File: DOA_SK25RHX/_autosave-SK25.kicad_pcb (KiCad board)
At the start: 2 copper layers, 29.2 x 29.2 mm, 44 parts, among them J1 Imput-, J2 Input+, J3 V+, J4 Output, J5 V-, J6 GND, Q1 BC560C, Q10 BD140, Q2 KSA992, Q3 KSA992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

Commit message: crude placement
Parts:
- D3: footprint LED_THT:LED_D5.0mm -> LED_THT:LED_D3.0mm
- Q10, Q9: footprint Package_TO_SOT_THT:TO-220-3_Vertical -> TAC:to225_std
- moved C2 91.7 mm to (181.6, 77.5), turned to 180 degrees
- moved D5 90.5 mm to (163.8, 115.6), turned to 180 degrees
- moved Q10 76.8 mm to (158.9, 84.5)
- moved D6 74.0 mm to (154.3, 72.4)
- moved Q9 68.9 mm to (158.8, 106.0), turned to 180 degrees
- moved R9 68.3 mm to (171.4, 108.0), turned to 90 degrees
- moved R10 67.3 mm to (177.2, 98.4), turned to 90 degrees
- moved Q3 66.8 mm to (157.5, 92.7), turned to 270 degrees
- moved Q7 63.8 mm to (160.7, 102.9), turned to 90 degrees
- moved Q8 62.0 mm to (152.4, 95.2), turned to 90 degrees
- moved RV5 60.5 mm to (146.1, 77.5), turned to 180 degrees
- moved R11 60.3 mm to (177.2, 92.1), turned to 90 degrees
- moved C1 59.8 mm to (165.1, 84.5), turned to 270 degrees
- moved Q6 57.6 mm to (161.3, 96.5)
- moved RV4 56.7 mm to (156.8, 78.1), turned to 180 degrees
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
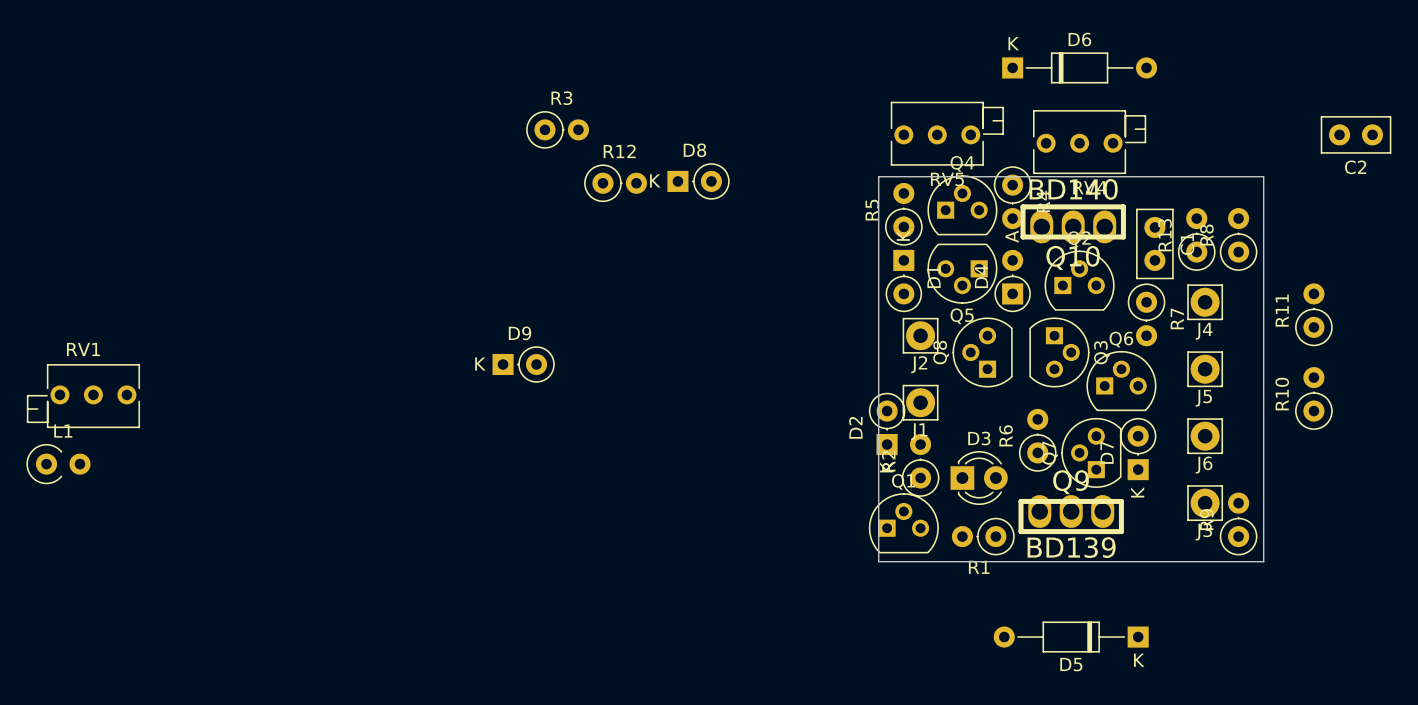
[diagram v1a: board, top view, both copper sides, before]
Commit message: abandoned layout. just TAC schematics for DOA socket
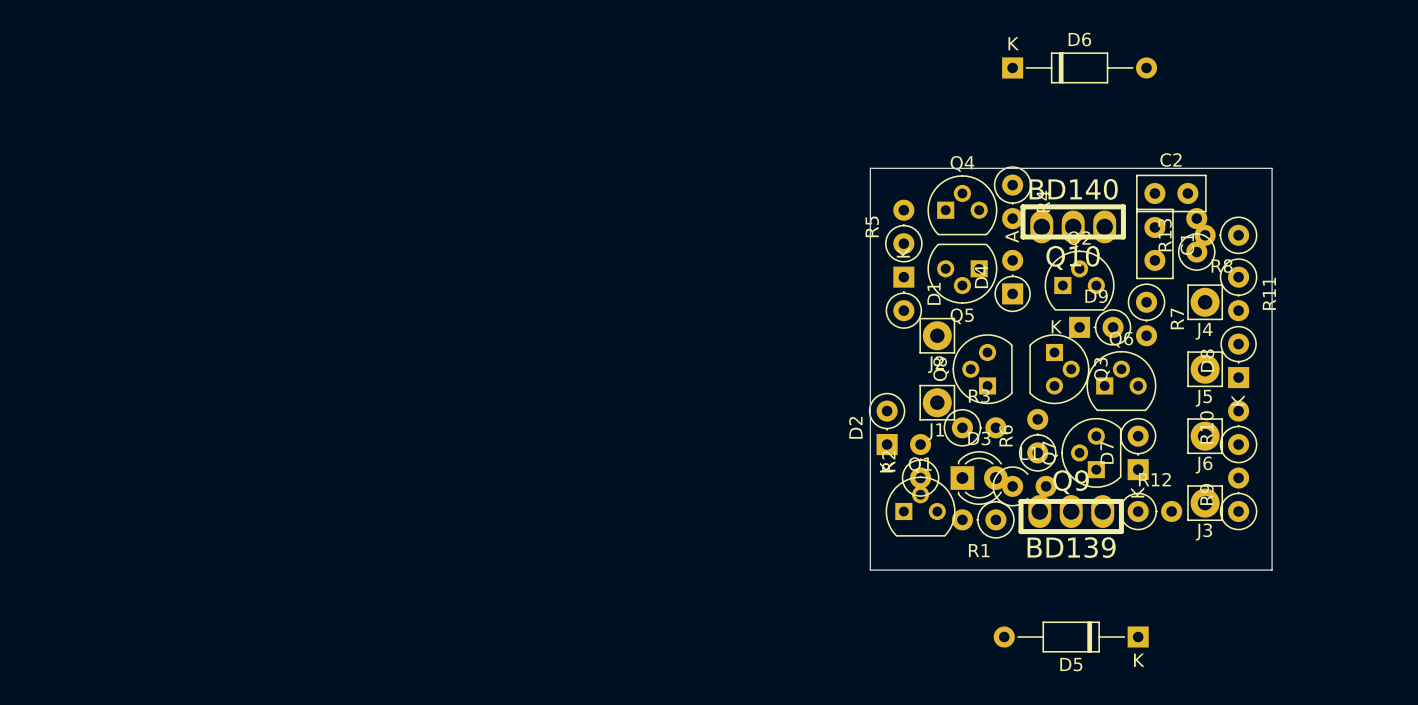
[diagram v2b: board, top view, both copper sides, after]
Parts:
- removed RV1, RV4, RV5: 2k, Potentiometer_THT:Potentiometer_Bourns_3266Z_Horizontal
- R1, R4, R5: value 470R -> 2k2
- moved L1 73.3 mm to (154.3, 104.1)
- moved R12 47.6 mm to (163.8, 106.0)
- moved D8 45.1 mm to (171.4, 95.9), turned to 90 degrees
- moved D9 43.8 mm to (159.4, 92.1)
- moved R3 38.9 mm to (150.5, 99.7)
- moved C2 17.1 mm to (165.1, 81.9), turned to 0 degrees
- moved R11 6.87 mm to (171.4, 88.3), turned to 270 degrees
- moved R10 6.25 mm to (171.4, 101.0)
- moved R9 1.91 mm to (171.4, 106.0)
- moved Q1 1.80 mm to (146.1, 106.0)
- moved J1 1.27 mm to (148.6, 97.8)
- moved J2 1.27 mm to (148.6, 92.7)
- moved Q3 1.27 mm to (157.5, 94.0)
- moved D1 1.27 mm to (146.1, 88.3)
- moved Q8 1.27 mm to (152.4, 96.5)
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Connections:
- R1 pad 2: Net-(R1-Pad2) -> Net-(Q1-Pad3)
- R4 pad 2: Net-(R4-Pad2) -> Net-(C2-Pad2)
- R5 pad 2: Net-(R5-Pad2) -> Net-(C2-Pad2)
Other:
- board size 29.2 x 29.2 mm -> 30.5 x 30.5 mm
